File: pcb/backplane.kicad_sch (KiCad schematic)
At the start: 7 parts, among them J10 XT60-F, J12 Conn_02x06_Odd_Even, J5 XT60-F, J6 XT60-F, J7 XT60-F, J8 XT60-F, J9 XT60-F

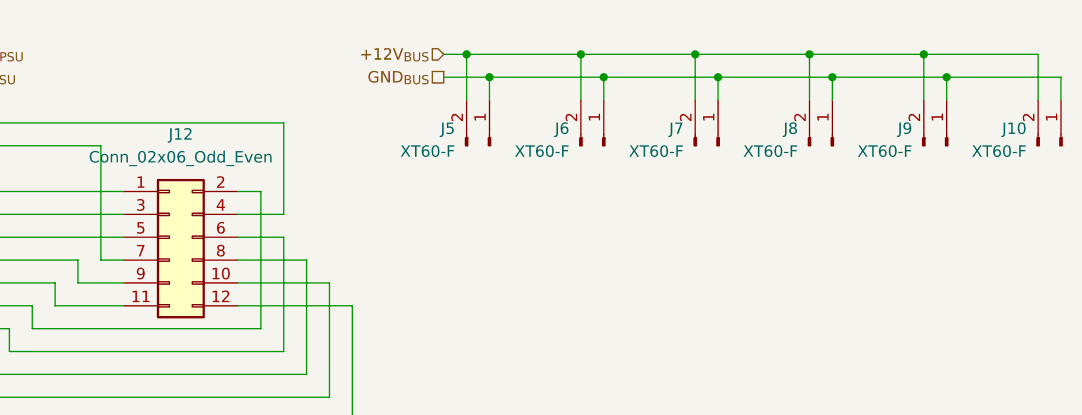
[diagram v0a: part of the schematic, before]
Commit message: feat: ERC and DRC in CI
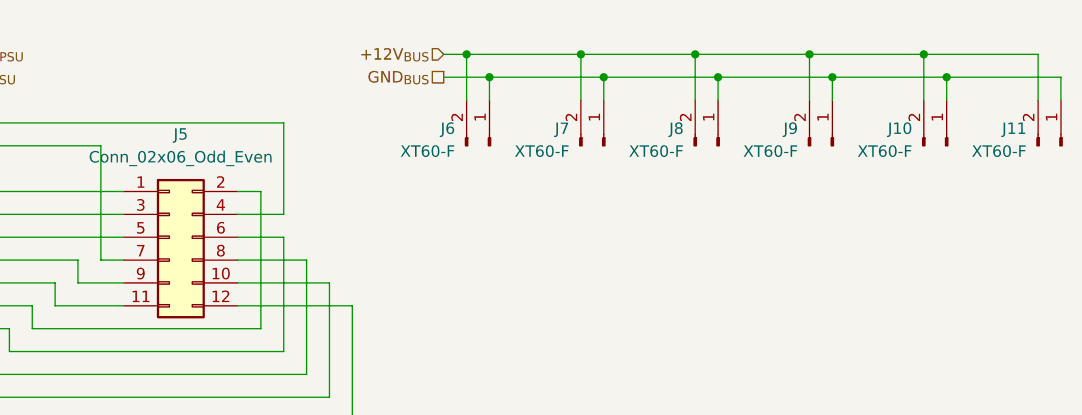
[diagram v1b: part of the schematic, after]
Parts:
- renumbered J9 to J10, J10 to J11, J12 to J5, J5 to J6, J6 to J7, J7 to J8, J8 to J9
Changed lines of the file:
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@@
 		(on_board yes)
 		(dnp no)
-		(property "Reference" "J10"
+		(property "Reference" "J11"
 			(at 173.99 55.2449 90)
 			(effects
@@
 			(project "pdu"
 				(path "/868598ab-f1a7-4d2b-9f5c-b3412115ebb5/83e31ad8-0e16-4075-8c02-9dd13935ed62"
-					(reference "J10")
+					(reference "J11")
 					(unit 1)
 				)
@@
 		(on_board yes)
 		(dnp no)
-		(property "Reference" "J6"
+		(property "Reference" "J7"
 			(at 123.19 55.2449 90)
 			(effects
@@
 			(project "pdu"
 				(path "/868598ab-f1a7-4d2b-9f5c-b3412115ebb5/83e31ad8-0e16-4075-8c02-9dd13935ed62"
-					(reference "J6")
+					(reference "J7")
 					(unit 1)
 				)
@@
 		(on_board yes)
 		(dnp no)
-		(property "Reference" "J5"
+		(property "Reference" "J6"
 			(at 110.49 55.2449 90)
 			(effects
@@
 			(project ""
 				(path "/868598ab-f1a7-4d2b-9f5c-b3412115ebb5/83e31ad8-0e16-4075-8c02-9dd13935ed62"
-					(reference "J5")
+					(reference "J6")
 					(unit 1)
 				)
@@
 		(on_board yes)
 		(dnp no)
-		(property "Reference" "J8"
+		(property "Reference" "J9"
 			(at 148.59 55.2449 90)
 			(effects
@@
 			(project "pdu"
 				(path "/868598ab-f1a7-4d2b-9f5c-b3412115ebb5/83e31ad8-0e16-4075-8c02-9dd13935ed62"
-					(reference "J8")
+					(reference "J9")
 					(unit 1)
 				)
@@
 		(on_board yes)
 		(dnp no)
-		(property "Reference" "J7"
+		(property "Reference" "J8"
 			(at 135.89 55.2449 90)
 			(effects
@@
 			(project "pdu"
 				(path "/868598ab-f1a7-4d2b-9f5c-b3412115ebb5/83e31ad8-0e16-4075-8c02-9dd13935ed62"
-					(reference "J7")
+					(reference "J8")
 					(unit 1)
 				)
@@
 		(on_board yes)
 		(dnp no)
-		(property "Reference" "J9"
+		(property "Reference" "J10"
 			(at 161.29 55.2449 90)
 			(effects
@@
 			(project "pdu"
 				(path "/868598ab-f1a7-4d2b-9f5c-b3412115ebb5/83e31ad8-0e16-4075-8c02-9dd13935ed62"
-					(reference "J9")
+					(reference "J10")
 					(unit 1)
 				)
@@
 		(on_board yes)
 		(dnp no)
-		(property "Reference" "J12"
+		(property "Reference" "J5"
 			(at 80.01 55.88 0)
 			(effects
@@
 			(project ""
 				(path "/868598ab-f1a7-4d2b-9f5c-b3412115ebb5/83e31ad8-0e16-4075-8c02-9dd13935ed62"
-					(reference "J12")
-					(unit 1)
-				)
+					(reference "J5")
+					(unit 1)
+				)

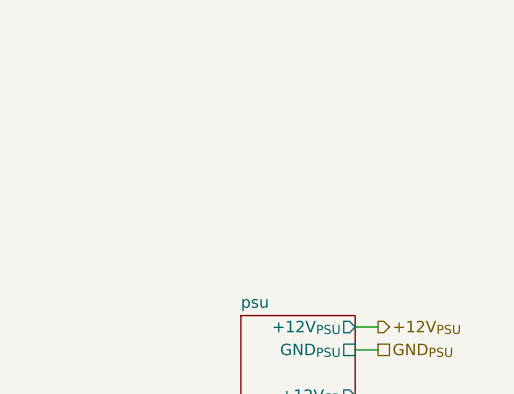
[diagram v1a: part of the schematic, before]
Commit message: fix: ERC, mark edge connector pins as passive
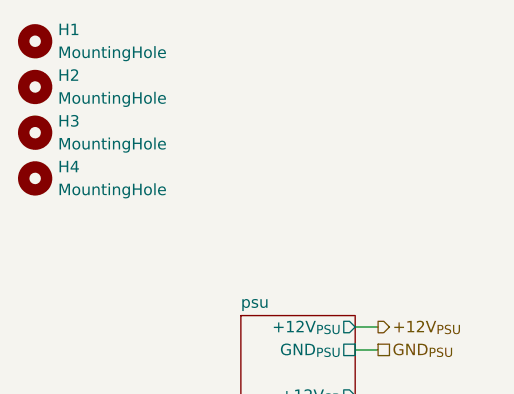
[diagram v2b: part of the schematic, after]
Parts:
- added H1, H2, H3, H4: MountingHole, MountingHole:MountingHole_3.2mm_M3, symbol Mechanical:MountingHole
